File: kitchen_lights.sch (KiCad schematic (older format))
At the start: 79 parts, among them IC1 MADW__ATTINY2313DIP/SO, IC2 MBI5168, IC3 7805MS, P1 CONN_8X2, P2 CONN_8X2, SW1 LPH_SW, SW2 LPH_SW, SW3 LPH_SW

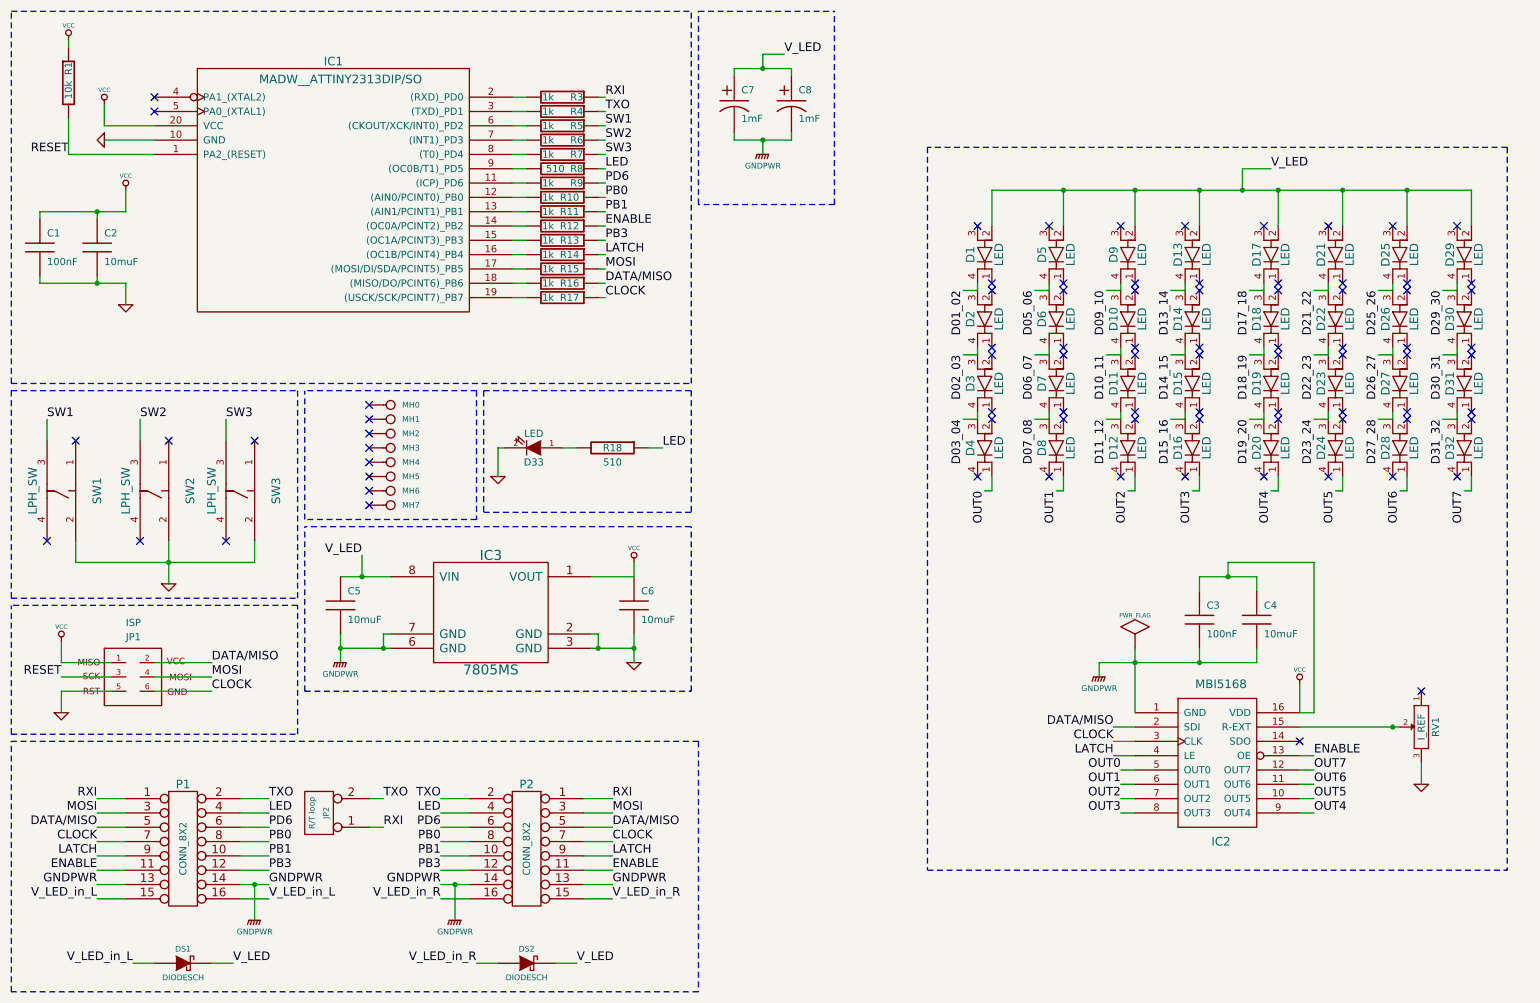
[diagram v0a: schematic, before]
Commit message: Added a whole lot of 0805 leds for status etc...
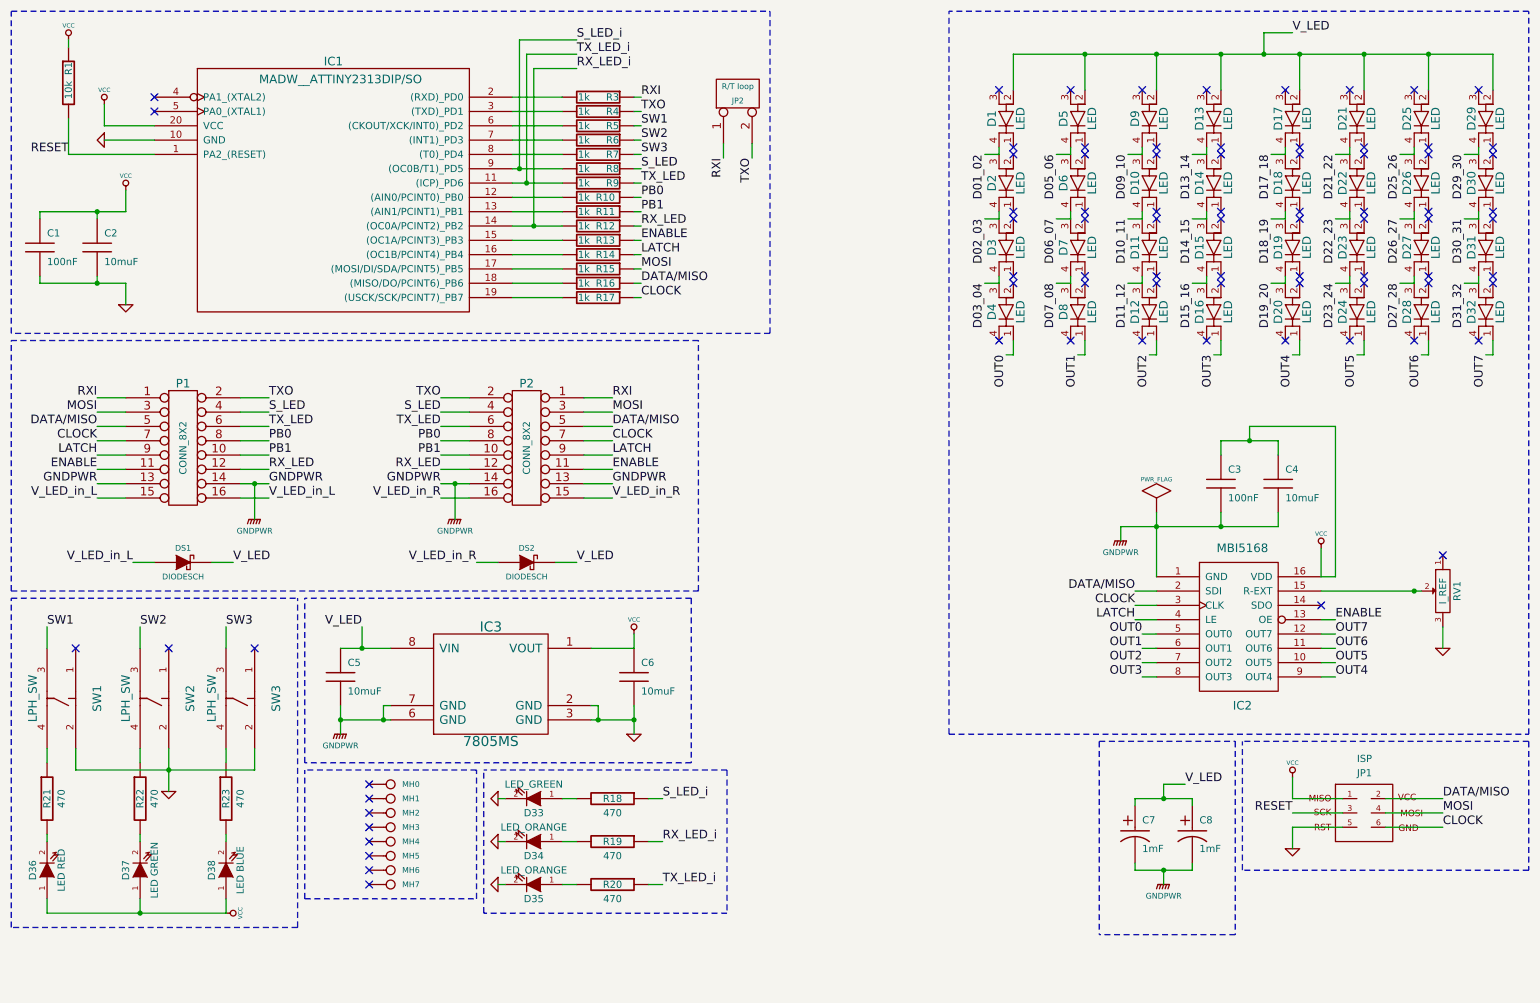
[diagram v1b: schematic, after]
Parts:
- added D34, D35: LED_ORANGE, symbol LED
- added D36: LED RED, symbol LED
- added D37: LED GREEN, symbol LED
- added D38: LED BLUE, symbol LED
- added R19, R20, R21, R22, R23: 470, symbol R
- D33: value LED -> LED_GREEN
- R18: value 510 -> 470
- R8: value 510 -> 1k
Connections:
- net ENABLE: now also R13.1; no longer R12.1
- net GND: now also D34.2 (K), D35.2 (K)
- net VCC: now also D36.1 (A), D37.1 (A), D38.1 (A)
- net at SW3.4: now also R23.1
- net at SW1.4: now also R21.1
- net at SW2.4: now also R22.1
- net TX_LED_i: now reaches IC1.11 ((ICP)_PD6), R9.2
- net TX_LED_i: now also R20.1
- net RX_LED_i: now reaches IC1.14 ((OC0A/PCINT2)_PB2), R12.2
- net RX_LED_i: now also R19.1
- net S_LED_i: now reaches IC1.9 ((OC0B/T1)_PD5), R8.2
- net S_LED_i: now also R18.1
- net LED renamed S_LED
- net S_LED: no longer R18.1
- net PB3 renamed RX_LED
- net RX_LED: now also R12.1; no longer R13.1
- net PD6 renamed TX_LED
- new net: D36.2 (K), R21.2
- new net: D37.2 (K), R22.2
- new net: D38.2 (K), R23.2
- new net: D34.1 (A), R19.2
- new net: D35.1 (A), R20.2
- no-connect marks 82 -> 79
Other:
- moved on the sheet: C3, C4, C5, C6, C7, C8, D1, D10, D11, D12, D13, D14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

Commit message: HOPEFULLY fixed the FRIGGIN' ISP header for good. 100$ of smoke ;-(
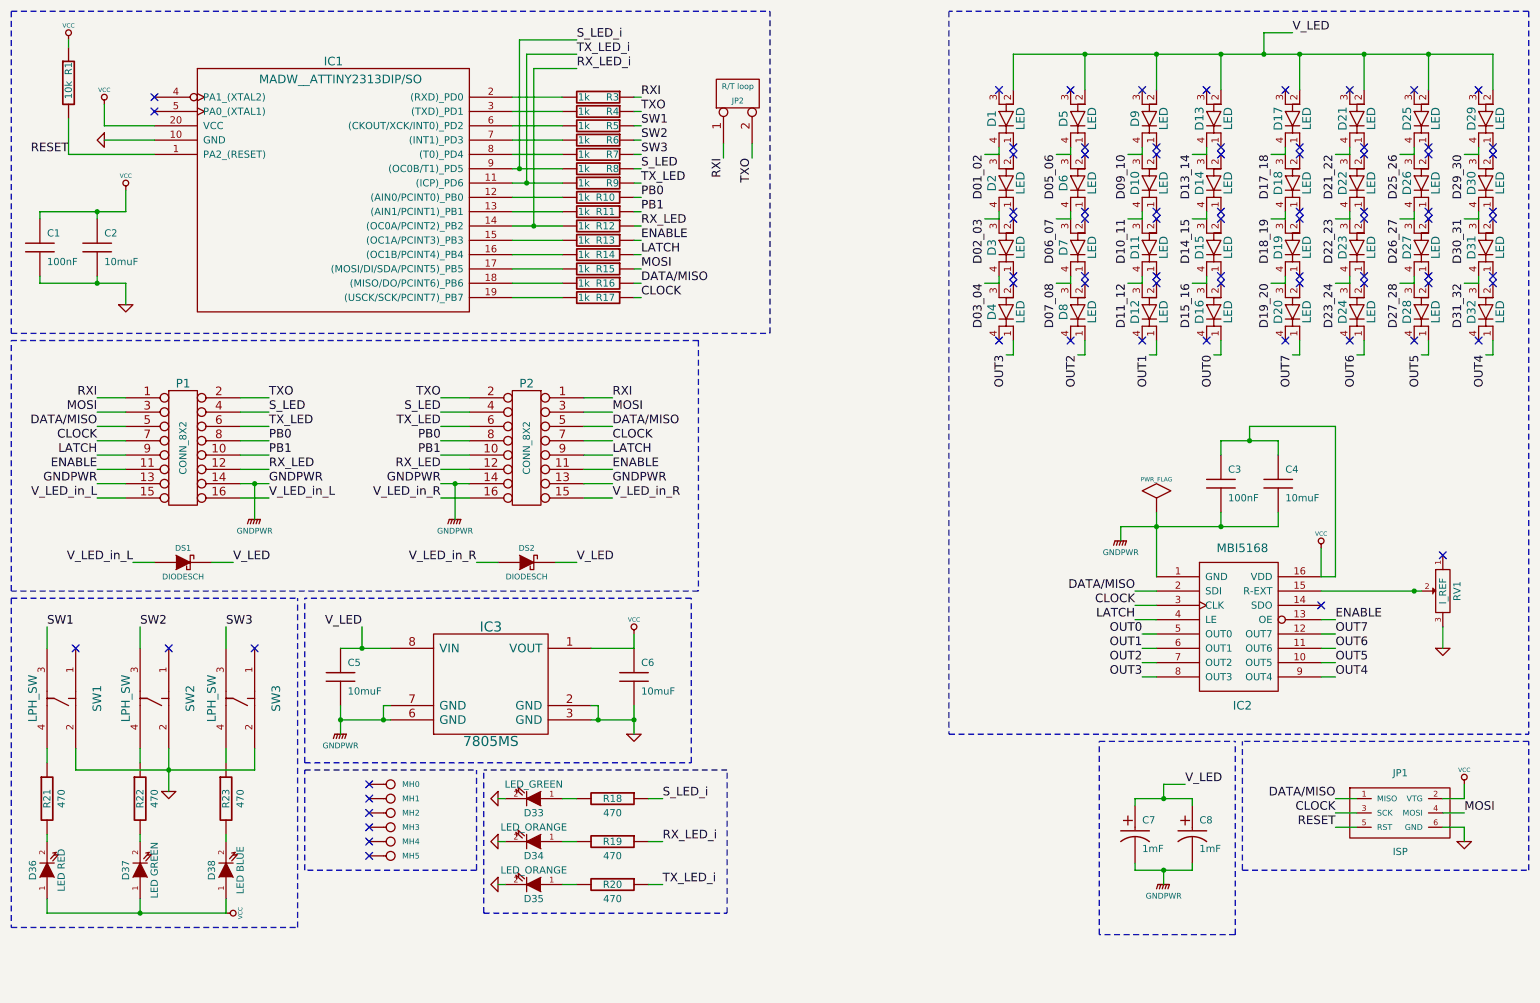
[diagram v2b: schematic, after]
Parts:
- removed JP1: ISP, atmel-AVR-ISP-6, symbol AVR-ISP-6
- removed MH6, MH7: CONN_1, symbol CONN_1
- added JP1: ISP, symbol MADW__AVR_ISP
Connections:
- net CLOCK: now also JP1.3 (SCK)
- net DATA/MISO: now also JP1.1 (MISO)
- net GND: now also JP1.6 (GND)
- net MOSI: now also JP1.4 (MOSI)
- net OUT0: now also D16.1; no longer D4.1
- net OUT1: now also D12.1; no longer D8.1
- net OUT2: now also D8.1; no longer D12.1
- net OUT3: now also D4.1; no longer D16.1
- net OUT4: now also D32.1; no longer D20.1
- net OUT5: now also D28.1; no longer D24.1
- net OUT6: now also D24.1; no longer D28.1
- net OUT7: now also D20.1; no longer D32.1
- net RESET: now also JP1.5 (RST)
- net VCC: now also JP1.2 (VTG)
- no-connect marks 79 -> 77
